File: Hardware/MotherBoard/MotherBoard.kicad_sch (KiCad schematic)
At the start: 19 parts, among them J11 CLOCK_SPD, J25 ATX-24, J3 CLOCK_SEL, J4 EXTRN_CLCK, Q1 2N3904, SW2 ON_OFF, SW3 RESET, U1 74HC590A, U10 NE555P, X1 ACO-16MHz

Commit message: Fix
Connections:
- net +5V: now also R3.1
- net PWR_OK: no longer R3.1
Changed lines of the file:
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@@
     (company "Romuald Rousseau")
   )
+  (bus_alias "A11" (members "A11"))
   (bus_alias "A12" (members "A12"))
-  (bus_alias "A11" (members "A11"))
   (junction (at 177.8 104.14) (diameter 0) (color 0 0 0 0)
   )
@@
   (junction (at 39.37 185.42) (diameter 1.016) (color 0 0 0 0)
   )
+  (junction (at 78.74 158.75) (diameter 0) (color 0 0 0 0)
+  )
   (junction (at 175.26 53.34) (diameter 0) (color 0 0 0 0)
   )
@@
   (junction (at 177.8 55.88) (diameter 0) (color 0 0 0 0)
   )
+  (junction (at 64.77 158.75) (diameter 0) (color 0 0 0 0)
+  )
   (junction (at 172.72 99.06) (diameter 0) (color 0 0 0 0)
   )
@@
   )
   (junction (at 127 104.14) (diameter 1.016) (color 0 0 0 0)
-  )
-  (junction (at 78.74 165.1) (diameter 0) (color 0 0 0 0)
   )
   (junction (at 74.93 39.37) (diameter 0) (color 0 0 0 0)
@@
     (stroke (width 0) (type default))
   )
+  (wire (pts (xy 39.37 158.75) (xy 64.77 158.75))
+    (stroke (width 0) (type default))
+  )
   (wire (pts (xy 180.34 106.68) (xy 180.34 58.42))
     (stroke (width 0) (type default))
@@
     (stroke (width 0) (type solid))
   )
-  (wire (pts (xy 78.74 154.94) (xy 78.74 165.1))
+  (wire (pts (xy 78.74 154.94) (xy 78.74 158.75))
     (stroke (width 0) (type solid))
   )
@@
     (stroke (width 0) (type solid))
   )
+  (wire (pts (xy 64.77 158.75) (xy 78.74 158.75))
+    (stroke (width 0) (type default))
+  )
   (wire (pts (xy 99.695 124.46) (xy 99.695 125.73))
     (stroke (width 0) (type default))
   )
-  (wire (pts (xy 64.77 165.1) (xy 78.74 165.1))
-    (stroke (width 0) (type default))
-  )
   (wire (pts (xy 116.84 129.54) (xy 116.84 134.62))
     (stroke (width 0) (type solid))
@@
     (stroke (width 0) (type dash))
   )
-  (wire (pts (xy 39.37 154.94) (xy 39.37 161.29))
-    (stroke (width 0) (type solid))
-  )
-  (wire (pts (xy 36.83 154.94) (xy 39.37 154.94))
-    (stroke (width 0) (type default))
-  )
   (wire (pts (xy 76.2 129.54) (xy 76.2 130.81))
     (stroke (width 0) (type solid))
@@
     (stroke (width 0) (type default))
   )
-  (wire (pts (xy 64.77 181.61) (xy 64.77 165.1))
+  (wire (pts (xy 64.77 158.75) (xy 64.77 181.61))
     (stroke (width 0) (type default))
   )
@@
     (stroke (width 0) (type default))
   )
-  (wire (pts (xy 78.74 165.1) (xy 78.74 166.37))
+  (wire (pts (xy 78.74 158.75) (xy 78.74 166.37))
     (stroke (width 0) (type solid))
   )
@@
   (wire (pts (xy 177.8 140.97) (xy 177.8 104.14))
     (stroke (width 0) (type default))
+  )
+  (wire (pts (xy 39.37 158.75) (xy 39.37 161.29))
+    (stroke (width 0) (type solid))
   )
   (wire (pts (xy 219.71 111.76) (xy 240.03 111.76))
@@
     (effects (font (size 1.27 1.27)) (justify left bottom))
   )
-  (global_label "PWR_OK" (shape input) (at 36.83 154.94 180) (fields_autoplaced)
-    (effects (font (size 1.27 1.27)) (justify right))
-    (property "Intersheetrefs" "${INTERSHEET_REFS}" (at 26.1902 154.94 0)
-      (effects (font (size 1.27 1.27)) (justify right) hide)
-    )
-  )
   (global_label "ECLOCK" (shape input) (at 119.38 127 180)

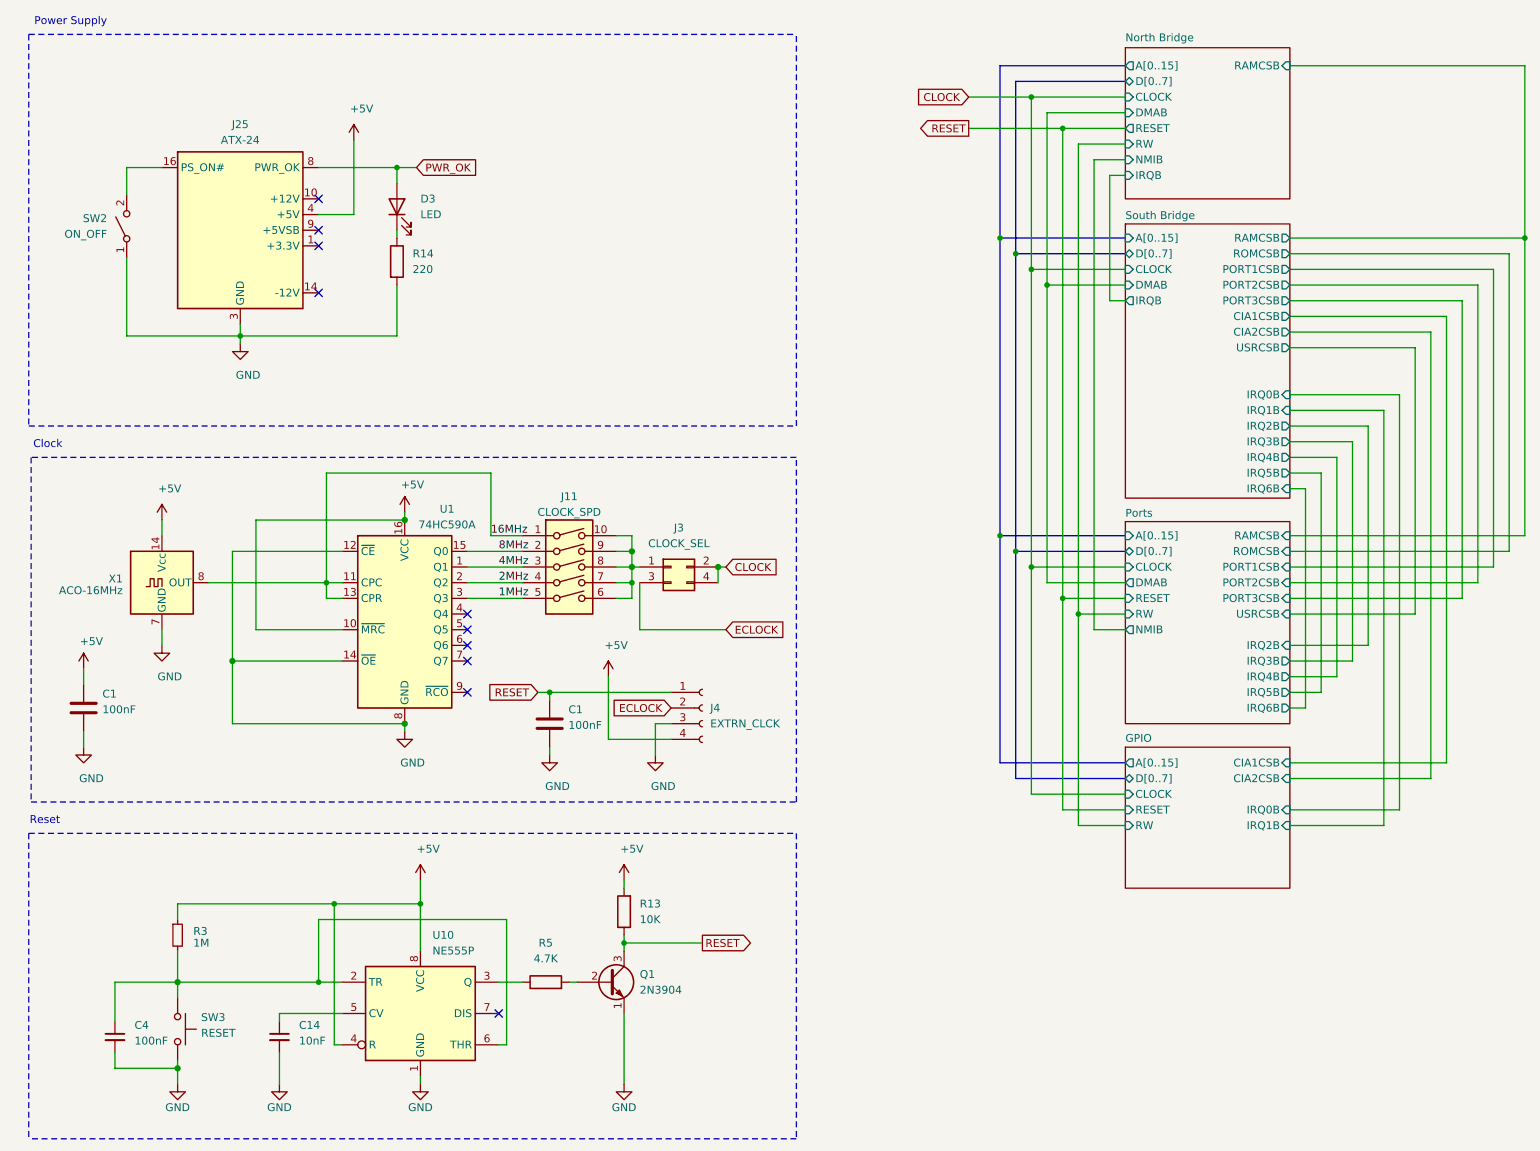
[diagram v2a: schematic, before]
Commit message: feat: modify mother board for paging and dma
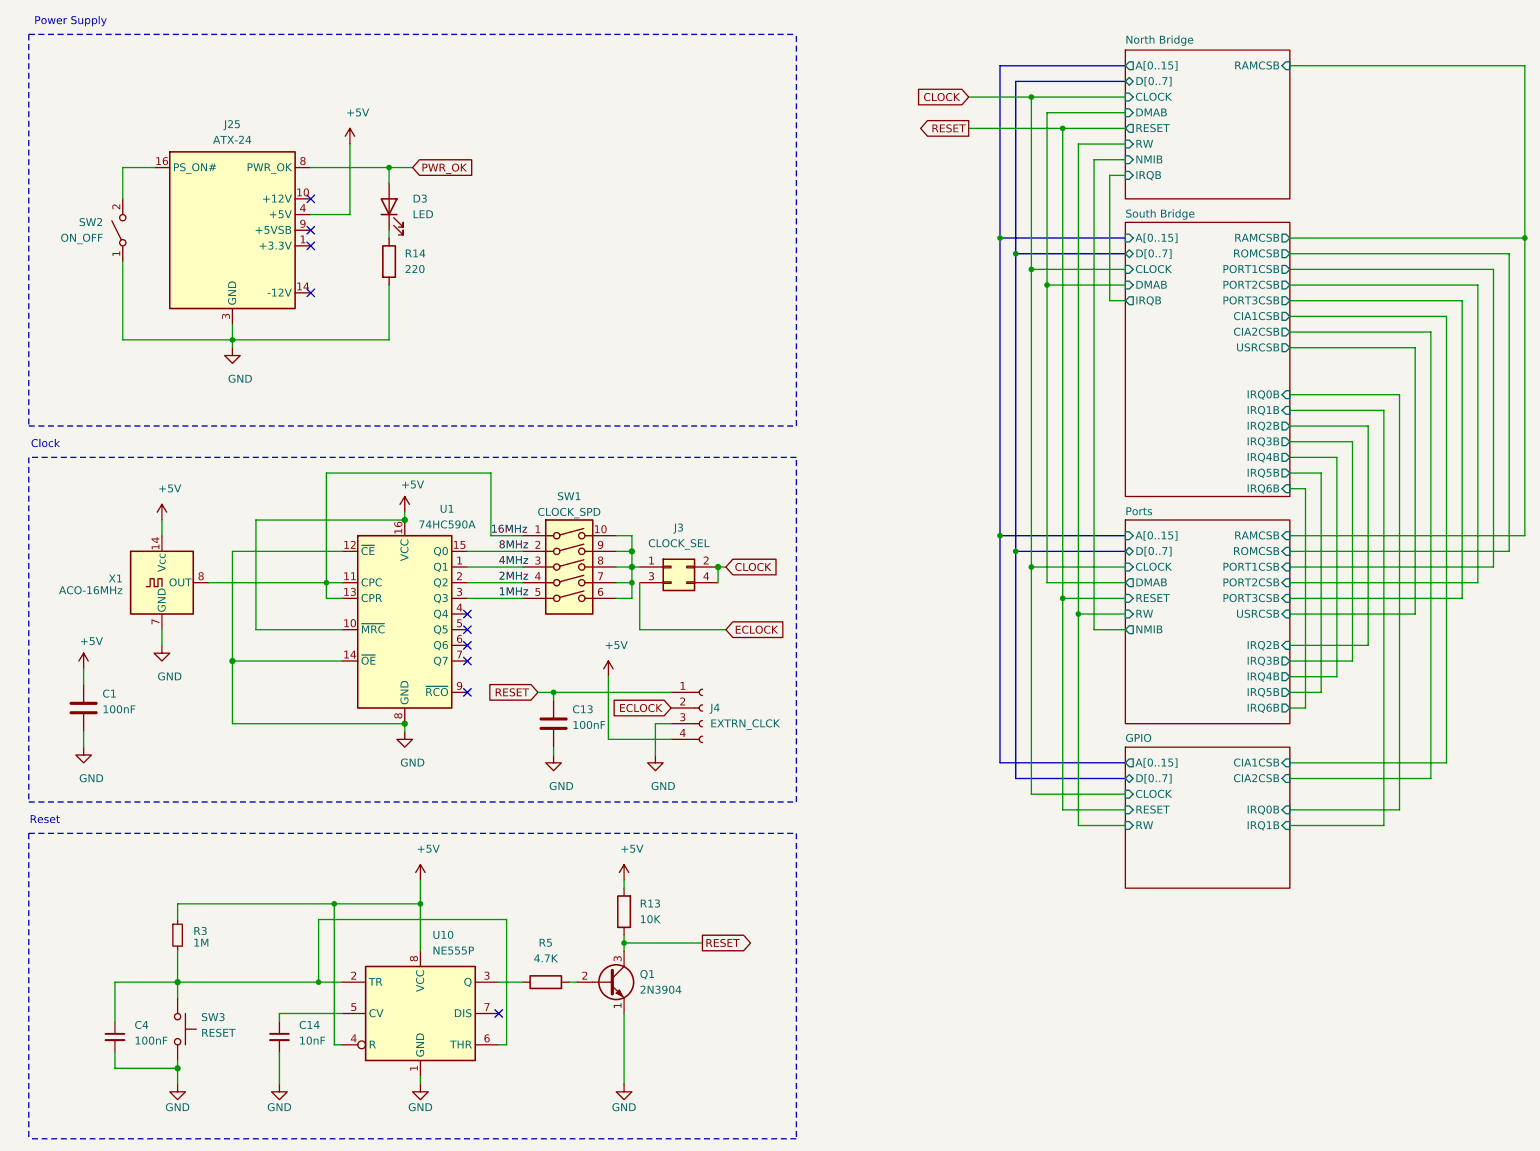
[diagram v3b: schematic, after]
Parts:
- renumbered C1 to C13, J11 to SW1
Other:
- moved on the sheet: C13, D3, J25, R14, SW2
